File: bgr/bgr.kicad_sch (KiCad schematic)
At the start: 17 parts, among them M1 eSim_MOS_P, M2 eSim_MOS_N, M3 eSim_MOS_P, M4 eSim_MOS_P, M5 eSim_MOS_P, Q1 eSim_NPN, Q2 eSim_NPN, Q3 eSim_NPN, Q4 eSim_NPN, Q5 eSim_NPN, Q6 eSim_NPN, Q7 eSim_NPN, Q8 eSim_NPN, Q9 eSim_NPN

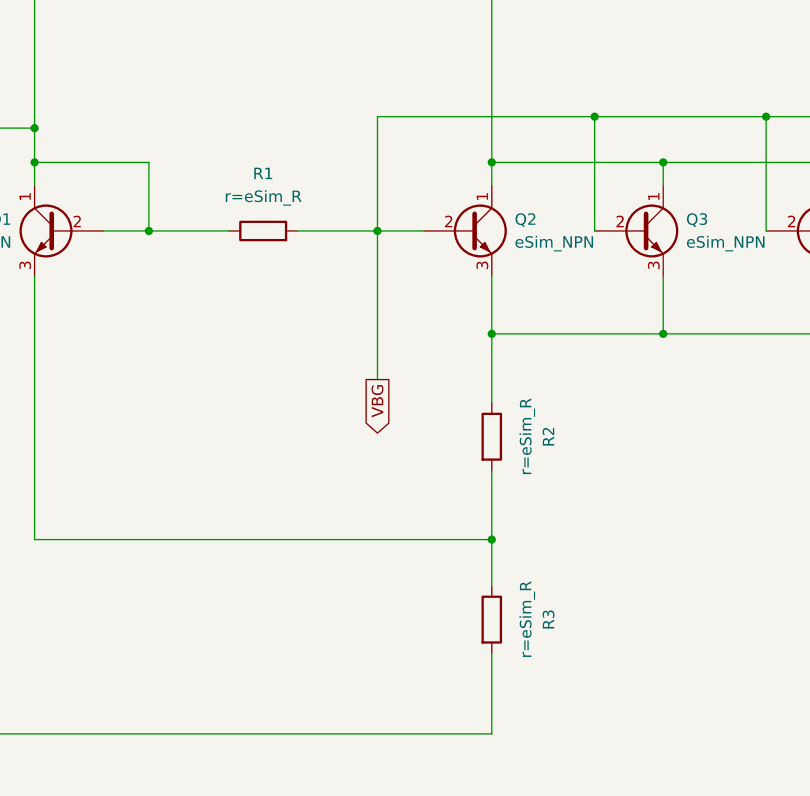
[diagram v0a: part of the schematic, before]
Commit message: schematic update
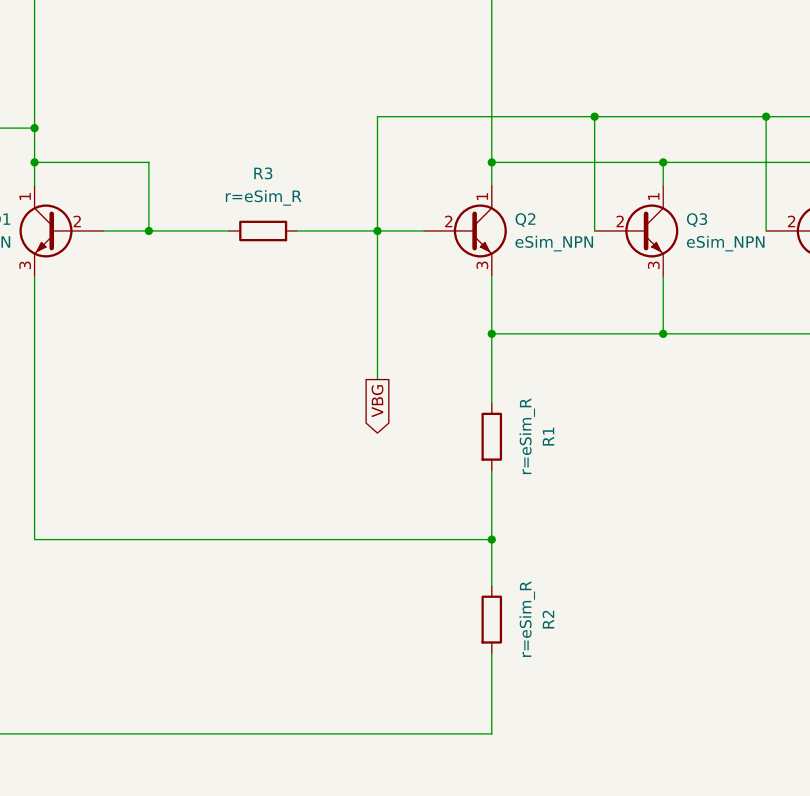
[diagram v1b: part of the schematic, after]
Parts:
- renumbered R2 to R1, R3 to R2, R1 to R3
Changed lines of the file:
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@@
 		(on_board yes)
 		(dnp no)
-		(property "Reference" "R3"
+		(property "Reference" "R2"
 			(at 140.97 146.05 0)
 			(effects
@@
 			(project "bgr"
 				(path "/7802ef7c-e287-4009-8282-24d37a852567"
-					(reference "R3")
+					(reference "R2")
 					(unit 1)
 				)
@@
 		(dnp no)
 		(fields_autoplaced yes)
-		(property "Reference" "R1"
+		(property "Reference" "R3"
 			(at 109.22 96.52 0)
 			(effects
@@
 			(project ""
 				(path "/7802ef7c-e287-4009-8282-24d37a852567"
-					(reference "R1")
+					(reference "R3")
 					(unit 1)
 				)
@@
 		(on_board yes)
 		(dnp no)
-		(property "Reference" "R2"
+		(property "Reference" "R1"
 			(at 140.97 125.73 0)
 			(effects
@@
 			(project ""
 				(path "/7802ef7c-e287-4009-8282-24d37a852567"
-					(reference "R2")
-					(unit 1)
-				)
+					(reference "R1")
+					(unit 1)
+				)
